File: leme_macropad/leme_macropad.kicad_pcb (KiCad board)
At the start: 4 copper layers, 99.9 x 63.9 mm, 90 parts, among them J1 OLED display, J2 USB_C_Receptacle_USB2.0_16P, SW1 SW_Push, SW2 SW_Push, SW3 SW_Push, SW4 RotaryEncoder_Switch, SW5 SW_Push, SW6 SW_Push, SW7 SW_Push, SW8 SW_Push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

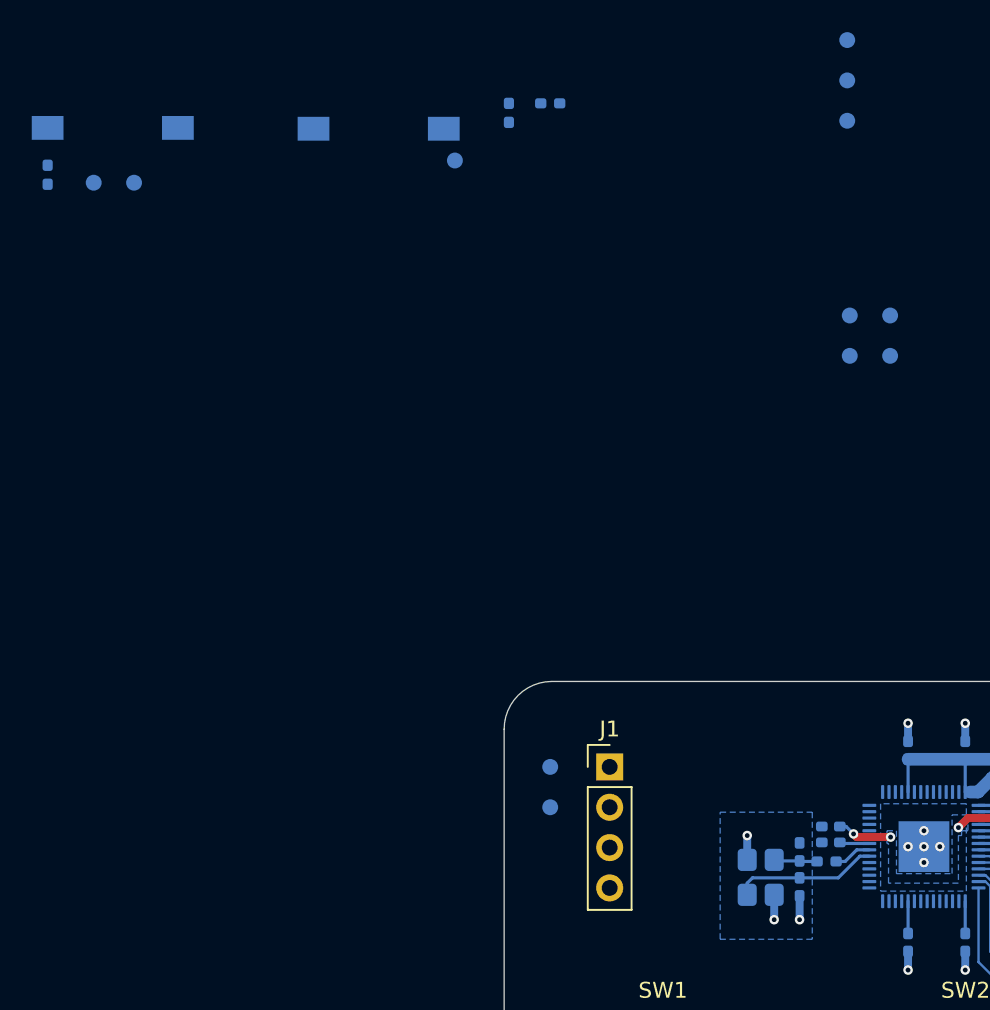
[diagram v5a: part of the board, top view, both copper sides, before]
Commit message: Routes SWD debug signals and reset
This required moving the decoupling capacitor for 1.1v.
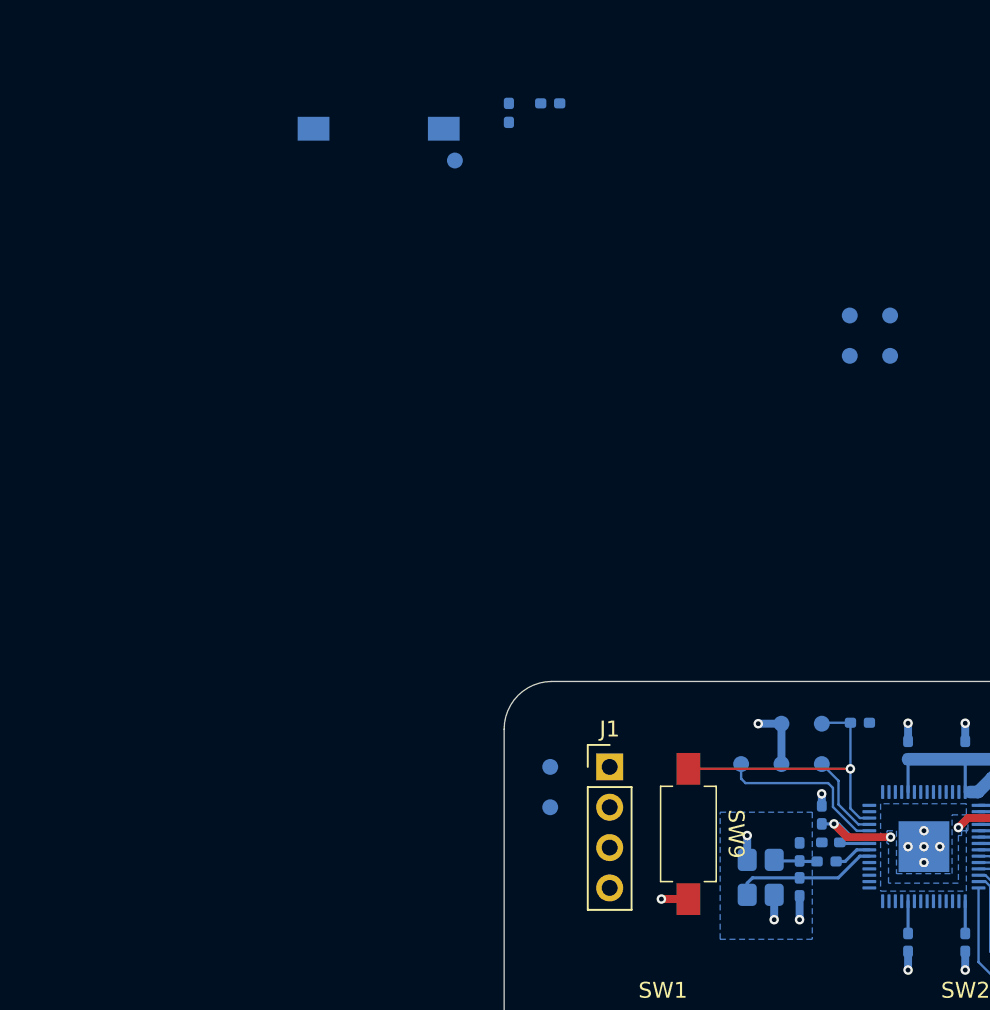
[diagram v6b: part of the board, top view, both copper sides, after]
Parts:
- SW9: moved to F.Cu
- moved R8 61.7 mm to (131.4, 67.6), turned to 180 degrees
- moved SW9 57.4 mm to (120.6, 74.6), turned to -90 degrees
- moved TP18 57.1 mm to (129.0, 67.7), turned to 0 degrees
- moved TP17 53.1 mm to (126.5, 67.7), turned to 0 degrees
- moved TP11 46.1 mm to (123.9, 70.2), turned to 90 degrees
- moved TP12 43.2 mm to (126.5, 70.2), turned to 90 degrees
- moved TP13 40.5 mm to (129.0, 70.2), turned to 90 degrees
- moved C14 0.93 mm to (129.0, 73.4), turned to 90 degrees
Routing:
- net ~{RESET}: track 0.00 -> 18.9 mm, vias 0 -> 1
- net SWCLK: track 0.00 -> 11.1 mm
- net GND: track 26.7 -> 33.2 mm, vias 25 -> 28
- net SWDIO: track 0.00 -> 5.44 mm
- net +1V1: track 17.3 -> 20.0 mm

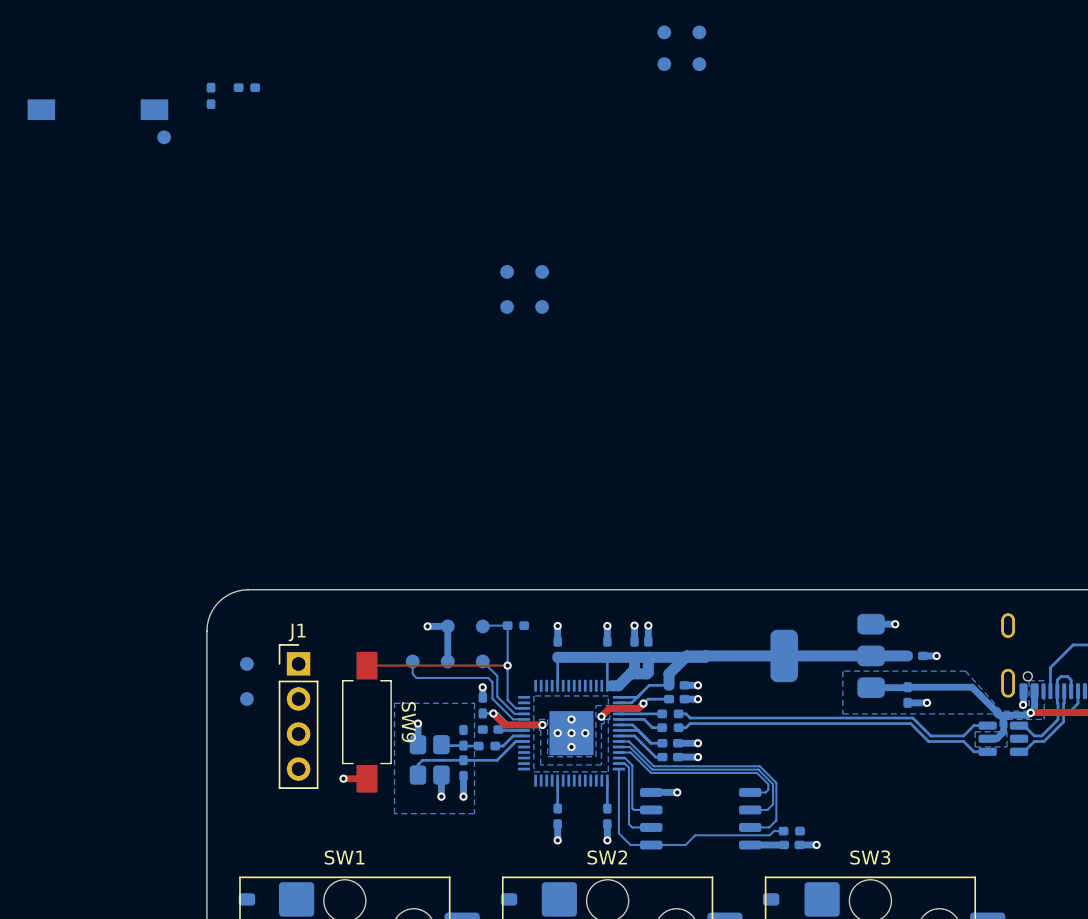
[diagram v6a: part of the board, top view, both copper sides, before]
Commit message: Routes "USB boot" button
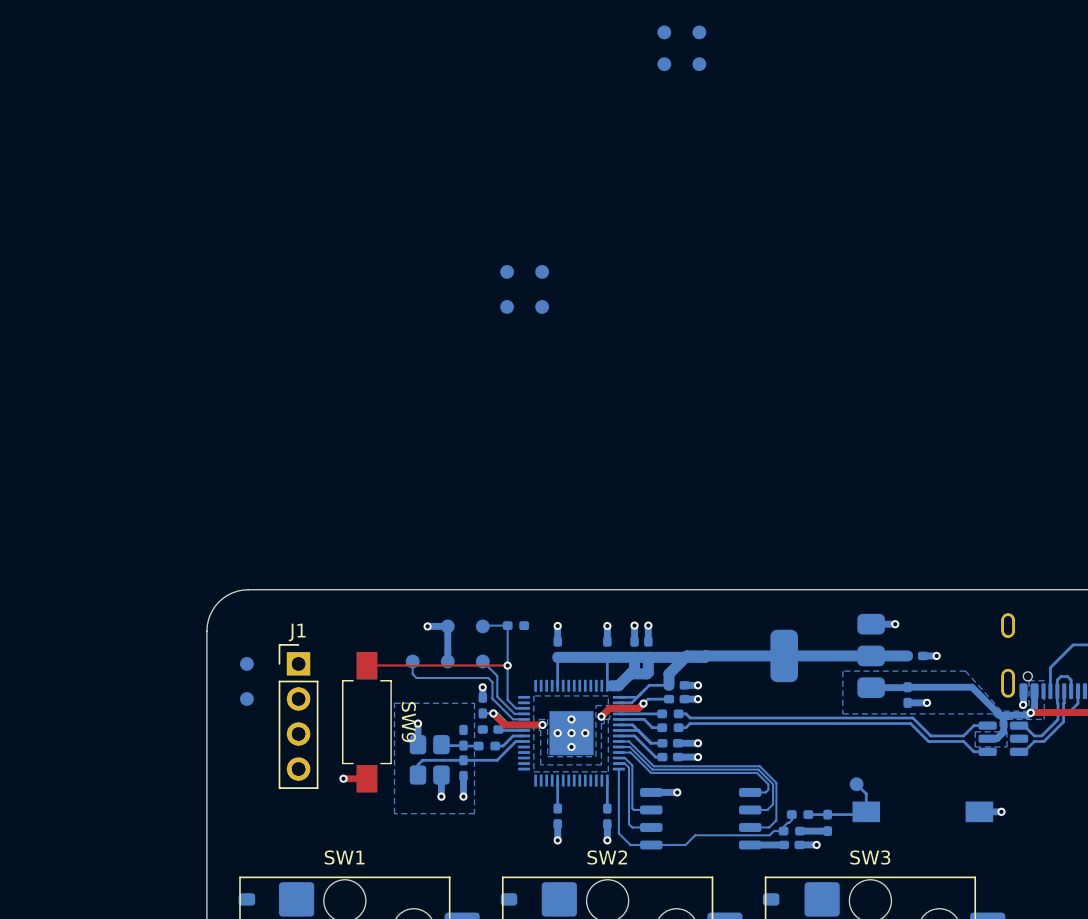
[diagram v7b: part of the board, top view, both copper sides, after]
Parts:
- moved SW8 78.5 mm to (160.9, 81.1), turned to 0 degrees
- moved R1 69.1 mm to (154.0, 81.9)
- moved TP0 68.7 mm to (156.1, 79.1), turned to 0 degrees
- moved R0 66.2 mm to (152.0, 81.3), turned to 180 degrees
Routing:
- net ~{USB BOOT}: track 0.00 -> 6.58 mm
- net +3.3V: track 59.7 -> 61.7 mm
- net GND: track 33.2 -> 34.8 mm, vias 28 -> 29
- net QSPI_SS: track 17.4 -> 18.9 mm
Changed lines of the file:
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@@
 	(footprint "leme_macropad:CK_PTS636_SK43_SMTR_LFS"
 		(layer "B.Cu")
-		(at 101.1 30.2025 180)
+		(at 160.9 81.1)
 		(descr "SMT SPST pushbutton")
 		(tags "button pushbutton SPST")
 		(property "Reference" "SW8"
-			(at 0 3 0)
+			(at 0 3 180)
 			(unlocked yes)
 			(layer "B.SilkS")
@@
 		)
 		(property "Value" "SW_Push"
-			(at 0 -2.75 0)
+			(at 0 -2.75 180)
 			(unlocked yes)
 			(layer "B.Fab")
@@
 		)
 		(property "Datasheet" "~"
-			(at 0 0 0)
+			(at 0 0 180)
 			(unlocked yes)
 			(layer "B.Fab")
@@
 		)
 		(property "Description" "Push button switch, generic, two pins"
-			(at 0 0 0)
+			(at 0 0 180)
 			(unlocked yes)
 			(layer "B.Fab")
@@
 		(attr smd)
 		(fp_line
-			(start 3 1.75)
-			(end 3 1)
+			(start -3 -1.75)
+			(end -3 -1)
 			(stroke
 				(width 0.1)
@@
 		)
 		(fp_line
-			(start 3 -1)
-			(end 3 -1.75)
+			(start -3 1)
+			(end -3 1.75)
 			(stroke
 				(width 0.1)
@@
 		)
 		(fp_line
-			(start 3 -1.75)
-			(end -3 -1.75)
+			(start -3 1.75)
+			(end 3 1.75)
 			(stroke
 				(width 0.1)
@@
 		)
 		(fp_line
-			(start -3 1.75)
-			(end 3 1.75)
+			(start 3 -1.75)
+			(end -3 -1.75)
 			(stroke
 				(width 0.1)
@@
 		)
 		(fp_line
-			(start -3 1)
-			(end -3 1.75)
+			(start 3 -1)
+			(end 3 -1.75)
 			(stroke
 				(width 0.1)
@@
 		)
 		(fp_line
-			(start -3 -1.75)
-			(end -3 -1)
+			(start 3 1.75)
+			(end 3 1)
 			(stroke
 				(width 0.1)
@@
 		)
 		(fp_rect
-			(start -1.25 0.5)
-			(end 1.25 -0.5)
+			(start -3 1.75)
+			(end 3 -1.75)
 			(stroke
 				(width 0.1)
@@
 		)
 		(fp_rect
-			(start -3 1.75)
-			(end 3 -1.75)
+			(start -1.25 0.5)
+			(end 1.25 -0.5)
 			(stroke
 				(width 0.1)
@@
 		)
 		(fp_text user "${REFERENCE}"
-			(at 0 -4.25 0)
+			(at 0 -4.25 180)
 			(unlocked yes)
 			(layer "B.Fab")
@@
 		)
 		(pad "1" smd rect
-			(at -4.1 0 180)
+			(at -4.1 0)
 			(size 2 1.5)
 			(layers "B.Cu" "B.Mask" "B.Paste")
@@
 		)
 		(pad "2" smd rect
-			(at 4.1 0 180)
+			(at 4.1 0)
 			(size 2 1.5)
 			(layers "B.Cu" "B.Mask" "B.Paste")
@@
 	(footprint "Resistor_SMD:R_0402_1005Metric_Pad0.72x0.64mm_HandSolder"
 		(layer "B.Cu")
-		(at 111.9 28.6025)
+		(at 152 81.3 180)
 		(descr "Resistor SMD 0402 (1005 Metric), square (rectangular) end terminal, IPC-7351 nominal with elongated pad for handsoldering. (Body size source: IPC-SM-782 page 72, https://www.pcb-3d.com/wordpress/wp-content/uploads/ipc-sm-782a_amendment_1_and_2.pdf), generated with kicad-footprint-generator")
 		(tags "resistor handsolder")
@@
 		(attr smd)
 		(fp_line
-			(start -0.167621 -0.38)
-			(end 0.167621 -0.38)
+			(start -0.167621 0.38)
+			(end 0.167621 0.38)
 			(stroke
 				(width 0.12)
@@
 		)
 		(fp_line
-			(start -0.167621 0.38)
-			(end 0.167621 0.38)
+			(start -0.167621 -0.38)
+			(end 0.167621 -0.38)
 			(stroke
 				(width 0.12)
@@
 		)
 		(fp_line
-			(start -1.11 -0.47)
-			(end -1.11 0.47)
+			(start 1.11 0.47)
+			(end 1.11 -0.47)
 			(stroke
 				(width 0.05)
@@
 		)
 		(fp_line
-			(start -1.11 0.47)
-			(end 1.11 0.47)
+			(start 1.11 -0.47)
+			(end -1.11 -0.47)
 			(stroke
 				(width 0.05)
@@
 		)
 		(fp_line
-			(start 1.11 -0.47)
-			(end -1.11 -0.47)
+			(start -1.11 0.47)
+			(end 1.11 0.47)
 			(stroke
 				(width 0.05)
@@
 		)
 		(fp_line
-			(start 1.11 0.47)
-			(end 1.11 -0.47)
+			(start -1.11 -0.47)
+			(end -1.11 0.47)
 			(stroke
 				(width 0.05)
@@
 		)
 		(fp_line
-			(start -0.525 -0.27)
-			(end -0.525 0.27)
+			(start 0.525 0.27)
+			(end 0.525 -0.27)
 			(stroke
 				(width 0.1)
@@
 		)
 		(fp_line
-			(start -0.525 0.27)
-			(end 0.525 0.27)
+			(start 0.525 -0.27)
+			(end -0.525 -0.27)
 			(stroke
 				(width 0.1)
@@
 		)
 		(fp_line
-			(start 0.525 -0.27)
-			(end -0.525 -0.27)
+			(start -0.525 0.27)
+			(end 0.525 0.27)
 			(stroke
 				(width 0.1)
@@
 		)
 		(fp_line
-			(start 0.525 0.27)
-			(end 0.525 -0.27)
+			(start -0.525 -0.27)
+			(end -0.525 0.27)
 			(stroke
 				(width 0.1)
@@
 		)
 		(pad "1" smd roundrect
-			(at -0.5975 0)
+			(at -0.5975 0 180)
 			(size 0.715 0.64)
 			(layers "B.Cu" "B.Mask" "B.Paste")
@@
 		)
 		(pad "2" smd roundrect
-			(at 0.5975 0)
+			(at 0.5975 0 180)
 			(size 0.715 0.64)
 			(layers "B.Cu" "B.Mask" "B.Paste")
@@
 	(footprint "Resistor_SMD:R_0402_1005Metric_Pad0.72x0.64mm_HandSolder"
 		(layer "B.Cu")
-		(at 109.3 29.2025 90)
+		(at 154 81.9 90)
 		(descr "Resistor SMD 0402 (1005 Metric), square (rectangular) end terminal, IPC-7351 nominal with elongated pad for handsoldering. (Body size source: IPC-SM-782 page 72, https://www.pcb-3d.com/wordpress/wp-content/uploads/ipc-sm-782a_amendment_1_and_2.pdf), generated with kicad-footprint-generator")
 		(tags "resistor handsolder")
@@
 	(footprint "TestPoint:TestPoint_Pad_D1.0mm"
 		(layer "B.Cu")
-		(at 105.9 32.2025 180)
+		(at 156.1 79.1)
 		(descr "SMD pad as test Point, diameter 1.0mm")
 		(tags "test point SMD pad")
@@
 		)
 		(property "Datasheet" "~"
-			(at 0 0 0)
+			(at 0 0 180)
 			(unlocked yes)
 			(layer "B.Fab")
@@
 		)
 		(property "Description" "test point"
-			(at 0 0 0)
+			(at 0 0 180)
 			(unlocked yes)
 			(layer "B.Fab")
@@
 		)
 		(pad "1" smd circle
-			(at 0 0 180)
+			(at 0 0)
 			(size 1 1)
 			(layers "B.Cu" "B.Mask")
@@
 	)
 	(via
+		(at 166.6 81.1)
+		(size 0.6)
+		(drill 0.3)
+		(layers "F.Cu" "B.Cu")
+		(net 2)
+	)
+	(via
 		(at 134.43 67.63)
 		(size 0.6)
@@
 	)
 	(segment
+		(start 165 81.1)
+		(end 166.6 81.1)
+		(width 0.5)
+		(layer "B.Cu")
+		(net 2)
+	)
+	(segment
 		(start 157.15 67.5)
 		(end 158.9 67.5)
@@
 	)
 	(segment
+		(start 153.9975 82.5)
+		(end 154 82.4975)
+		(width 0.5)
+		(layer "B.Cu")
+		(net 3)
+	)
+	(segment
 		(start 143.8 69.8)
 		(end 142.5 71.1)
@@
 	)
 	(segment
+		(start 151.9975 82.5)
+		(end 153.9975 82.5)
+		(width 0.5)
+		(layer "B.Cu")
+		(net 3)
+	)
+	(segment
 		(start 139.7 71.1)
 		(end 138.8375 71.9625)
@@
 	)
 	(segment
+		(start 151.2 81.9)
+		(end 151.4025 81.6975)
+		(width 0.15)
+		(layer "B.Cu")
+		(net 34)
+	)
+	(segment
 		(start 139.705 83.505)
 		(end 141.2125 83.505)
@@
 	)
 	(segment
+		(start 150.8025 82.1975)
+		(end 151.1 81.9)
+		(width 0.15)
+		(layer "B.Cu")
+		(net 34)
+	)
+	(segment
 		(start 144.4 82.8)
 		(end 149.8 82.8)
@@
 	)
 	(segment
+		(start 151.1 81.9)
+		(end 151.2 81.9)
+		(width 0.15)
+		(layer "B.Cu")
+		(net 34)
+	)
+	(segment
 		(start 143.695 83.505)
 		(end 144.4 82.8)
@@
 	)
 	(segment
+		(start 151.4025 81.6975)
+		(end 151.4025 81.3)
+		(width 0.15)
+		(layer "B.Cu")
+		(net 34)
+	)
+	(segment
+		(start 150.8025 82.5)
+		(end 150.8025 82.1975)
+		(width 0.15)
+		(layer "B.Cu")
+		(net 34)
+	)
+	(segment
 		(start 141.2125 83.505)
 		(end 143.695 83.505)
@@
 	)
 	(segment
+		(start 156.8 79.8)
+		(end 156.8 81.1)
+		(width 0.2)
+		(layer "B.Cu")
+		(net 35)
+	)
+	(segment
+		(start 152.5975 81.3)
+		(end 156.6 81.3)
+		(width 0.2)
+		(layer "B.Cu")
+		(net 35)
+	)
+	(segment
+		(start 156.1 79.1)
+		(end 156.8 79.8)
+		(width 0.2)
+		(layer "B.Cu")
+		(net 35)
+	)
+	(segment
+		(start 156.6 81.3)
+		(end 156.8 81.1)
+		(width 0.2)
+		(layer "B.Cu")
+		(net 35)
+	)
+	(segment
